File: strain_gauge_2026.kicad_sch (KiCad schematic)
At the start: 34 parts, among them J2 Conn_01x04_Socket, J3 Conn_01x04_Socket, J4 Conn_01x04_Socket, SW1 SW_DIP_x04, U1 NAU7802SGI, U2 LTC4316xDD

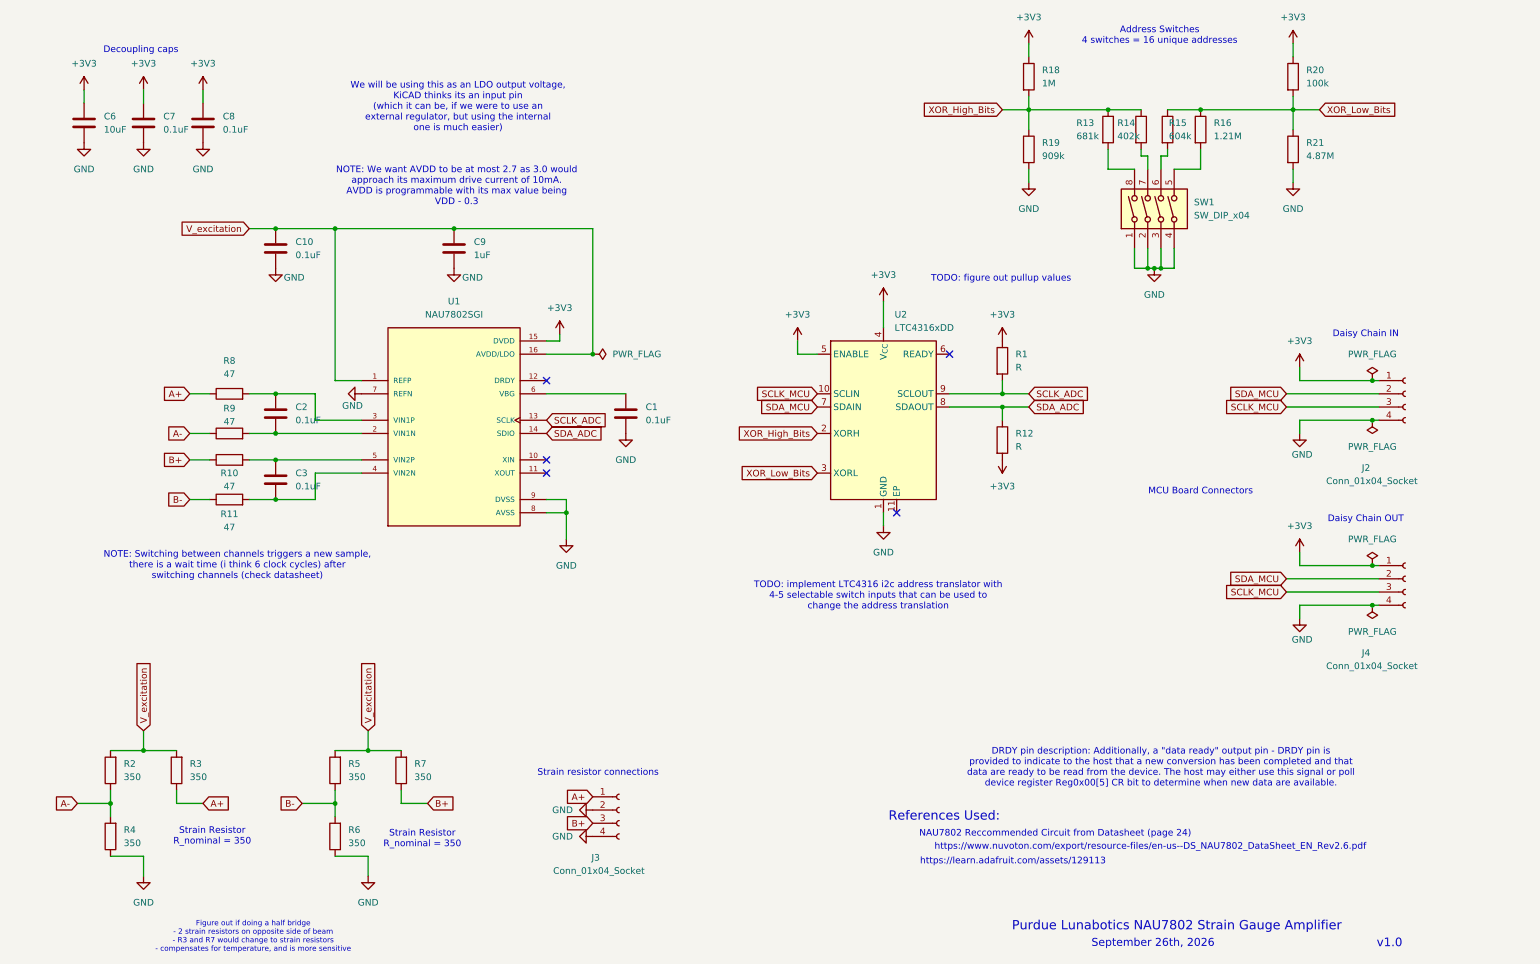
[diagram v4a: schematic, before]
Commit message: Removed LTC4316 from schematic
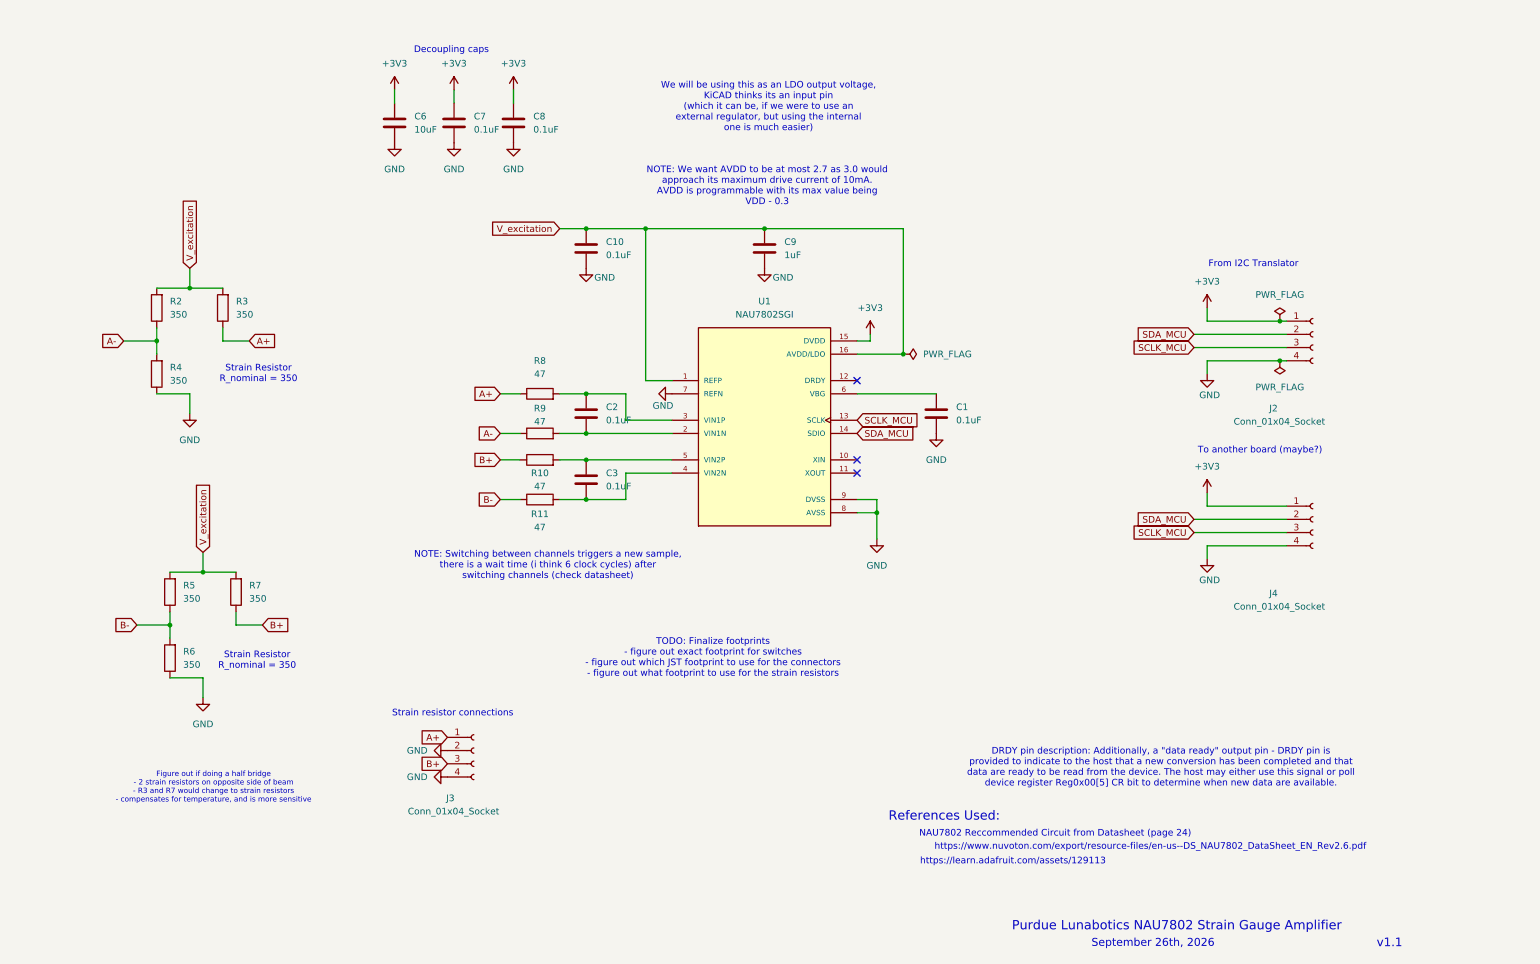
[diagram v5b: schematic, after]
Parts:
- removed R1, R12: R, symbol Device:R
- removed R13: 681k, symbol Device:R
- removed R14: 402k, symbol Device:R
- removed R15: 604k, symbol Device:R
- removed R16: 1.21M, symbol Device:R
- removed R18: 1M, symbol Device:R
- removed R19: 909k, symbol Device:R
- removed R20: 100k, symbol Device:R
- removed R21: 4.87M, symbol Device:R
- removed SW1: SW_DIP_x04, Button_Switch_THT:SW_NKK_GW12LJP, symbol Switch:SW_DIP_x04
- removed U2: LTC4316xDD, Package_DFN_QFN:DFN-10-1EP_3x3mm_P0.5mm_EP1.65x2.38mm, symbol Interface_Expansion:LTC4316xDD
- C1, C10, C2, C3, C7, C8, C9: footprint (none) -> Capacitor_SMD:C_0805_2012Metric_Pad1.18x1.45mm_HandSolder
- C6: footprint (none) -> Capacitor_THT:CP_Radial_D5.0mm_P2.50mm
- J2, J3, J4: footprint Package_DFN_QFN:QFN-20-1EP_5x5mm_P0.65mm_EP3.35x3.35mm -> Connector_PinHeader_2.54mm:PinHeader_1x04_P2.54mm_Vertical
- R10, R11, R2, R3, R4, R5, R6, R7, R8, R9: footprint (none) -> Resistor_SMD:R_0805_2012Metric_Pad1.20x1.40mm_HandSolder
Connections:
- net SCLK_ADC is gone; now on net SCLK_MCU: U1.13 (SCLK)
- net SDA_ADC is gone; now on net SDA_MCU: U1.14 (SDIO)
- no-connect marks 5 -> 3
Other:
- note added: "From I2C Translator"
- note added: "TODO: Finalize footprints - figure out exact footprint for switches - figure out which JST footprint to use for the connectors - figure out what footprint to use for the strain resistors"
- note added: "To another board (maybe?)"
- note added: "v1.1"
- note removed: "Address Switches 4 switches = 16 unique addresses"
- note removed: "Daisy Chain IN"
- note removed: "Daisy Chain OUT"
- note removed: "MCU Board Connectors"
- note removed: "TODO: figure out pullup values"
- note removed: "TODO: implement LTC4316 i2c address translator with 4-5 selectable switch inputs that can be used to change the address translation"
- note removed: "v1.0"
- moved on the sheet: C1, C10, C2, C3, C6, C7, C8, C9, J2, J3, J4, R10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

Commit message: Added optional Half/Quarter bridge connections
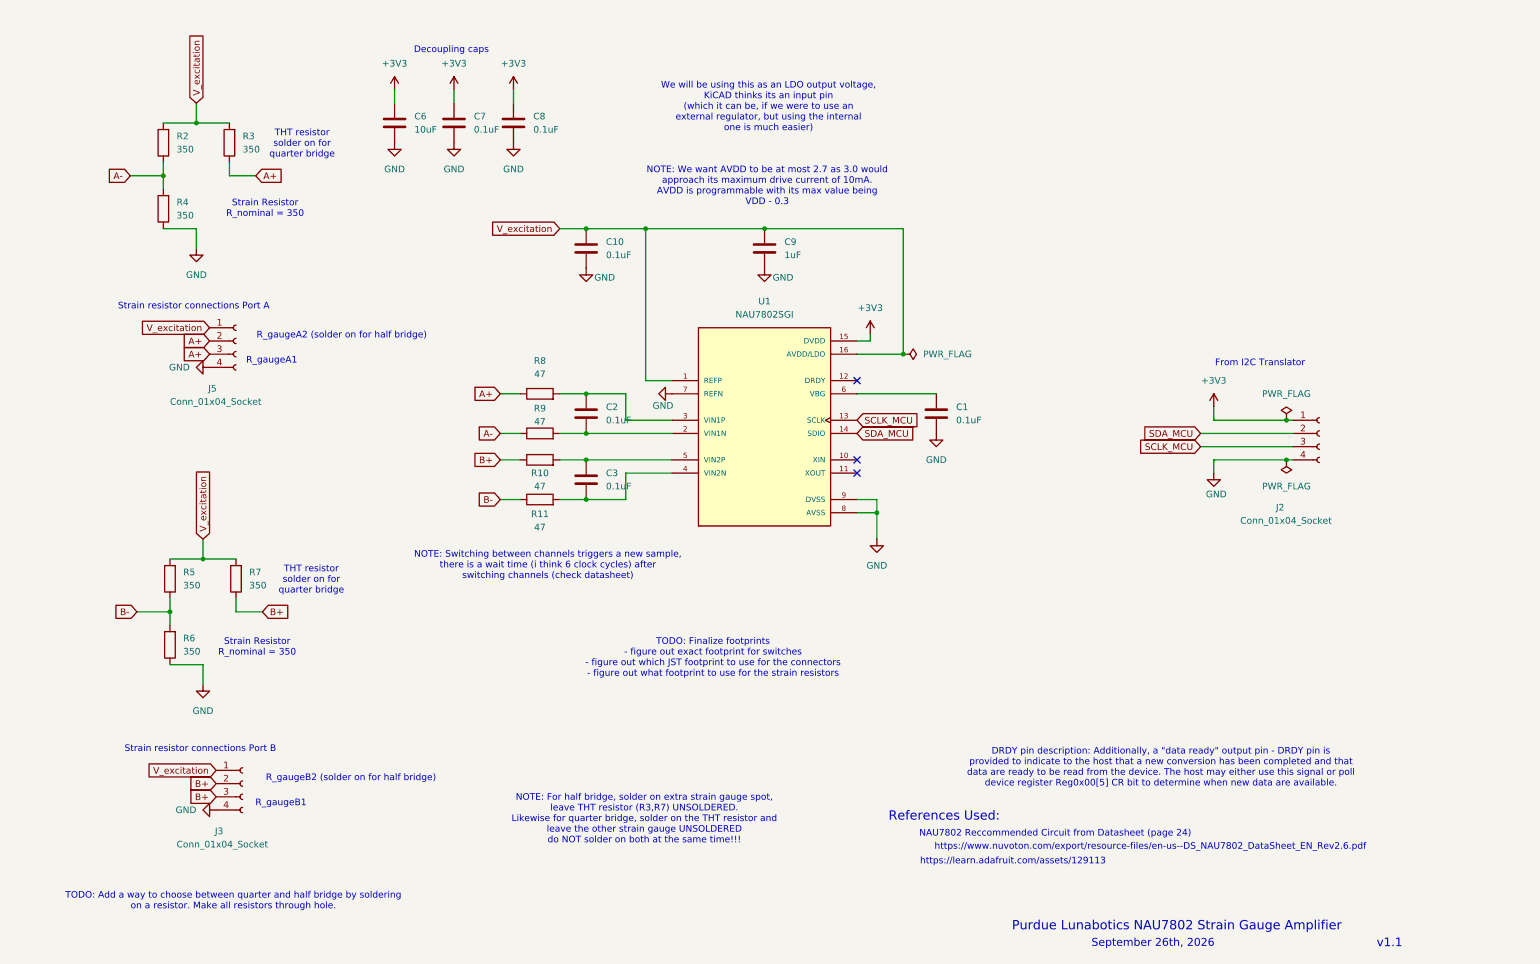
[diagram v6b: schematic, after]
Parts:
- removed J4: Conn_01x04_Socket, Connector_PinHeader_2.54mm:PinHeader_1x04_P2.54mm_Vertical, symbol Connector:Conn_01x04_Socket
- added J5: Conn_01x04_Socket, Connector_PinHeader_2.54mm:PinHeader_1x04_P2.54mm_Vertical, symbol Connector:Conn_01x04_Socket
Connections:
- net A+: now also J5.2 (Pin_2), J5.3 (Pin_3); no longer J3.1 (Pin_1)
- net B+: now also J3.2 (Pin_2)
- net GND: now also J5.4 (Pin_4); no longer J3.2 (Pin_2)
- net V_excitation: now also J3.1 (Pin_1), J5.1 (Pin_1)
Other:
- note added: "NOTE: For half bridge, solder on extra strain gauge spot, leave THT resistor (R3,R7) UNSOLDERED. Likewise for quarter bridge, solder on the THT resistor and leave the other strain gauge UNSOLDERED do NOT solder on both at the same time!!!"
- note added: "R_gaugeA1"
- note added: "R_gaugeA2 (solder on for half bridge)"
- note added: "R_gaugeB1"
- note added: "R_gaugeB2 (solder on for half bridge)"
- note added: "Strain resistor connections Port A"
- note added: "Strain resistor connections Port B"
- note added: "THT resistor solder on for quarter bridge"
- note added: "TODO: Add a way to choose between quarter and half bridge by soldering on a resistor. Make all resistors through hole."
- note removed: "Figure out if doing a half bridge - 2 strain resistors on opposite side of beam - R3 and R7 would change to strain resistors - compensates for temperature, and is more sensitive"
- note removed: "Strain resistor connections"
- note removed: "To another board (maybe?)"
- moved on the sheet: J2, J3, R2, R3, R4, R5, R6, R7

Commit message: Passives selected, footprints assigned accordingly
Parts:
- C6: footprint Capacitor_THT:CP_Radial_D5.0mm_P2.50mm -> Capacitor_THT:CP_Radial_D5.0mm_P2.00mm
- C9: footprint Capacitor_SMD:C_0805_2012Metric_Pad1.18x1.45mm_HandSolder -> Capacitor_THT:C_Rect_L7.0mm_W3.5mm_P5.00mm
- R10, R11, R2, R3, R4, R5, R6, R7, R8, R9: footprint Resistor_SMD:R_0805_2012Metric_Pad1.20x1.40mm_HandSolder -> Resistor_THT:R_Axial_DIN0207_L6.3mm_D2.5mm_P10.16mm_Horizontal
- U1: footprint strain_gauge_footprint_lib:SOIC127P600X175-16N -> Package_DIP:DIP-16_W7.62mm
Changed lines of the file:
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@@
 			)
 		)
-		(property "Footprint" "Resistor_SMD:R_0805_2012Metric_Pad1.20x1.40mm_HandSolder"
+		(property "Footprint" "Resistor_THT:R_Axial_DIN0207_L6.3mm_D2.5mm_P10.16mm_Horizontal"
 			(at 55.118 123.19 90)
 			(hide yes)
@@
 			)
 		)
-		(property "Footprint" "Resistor_SMD:R_0805_2012Metric_Pad1.20x1.40mm_HandSolder"
+		(property "Footprint" "Resistor_THT:R_Axial_DIN0207_L6.3mm_D2.5mm_P10.16mm_Horizontal"
 			(at 53.848 39.37 90)
 			(hide yes)
@@
 			)
 		)
-		(property "Footprint" "Resistor_SMD:R_0805_2012Metric_Pad1.20x1.40mm_HandSolder"
+		(property "Footprint" "Resistor_THT:R_Axial_DIN0207_L6.3mm_D2.5mm_P10.16mm_Horizontal"
 			(at 111.76 109.728 90)
 			(hide yes)
@@
 			)
 		)
-		(property "Footprint" "Capacitor_THT:CP_Radial_D5.0mm_P2.50mm"
+		(property "Footprint" "Capacitor_THT:CP_Radial_D5.0mm_P2.00mm"
 			(at 84.7852 39.37 0)
 			(hide yes)
@@
 			)
 		)
-		(property "Footprint" "Resistor_SMD:R_0805_2012Metric_Pad1.20x1.40mm_HandSolder"
+		(property "Footprint" "Resistor_THT:R_Axial_DIN0207_L6.3mm_D2.5mm_P10.16mm_Horizontal"
 			(at 41.148 39.37 90)
 			(hide yes)
@@
 			)
 		)
-		(property "Footprint" "Resistor_SMD:R_0805_2012Metric_Pad1.20x1.40mm_HandSolder"
+		(property "Footprint" "Resistor_THT:R_Axial_DIN0207_L6.3mm_D2.5mm_P10.16mm_Horizontal"
 			(at 42.418 135.89 90)
 			(hide yes)
@@
 			)
 		)
-		(property "Footprint" "Resistor_SMD:R_0805_2012Metric_Pad1.20x1.40mm_HandSolder"
+		(property "Footprint" "Resistor_THT:R_Axial_DIN0207_L6.3mm_D2.5mm_P10.16mm_Horizontal"
 			(at 111.76 97.028 90)
 			(hide yes)
@@
 			)
 		)
-		(property "Footprint" "Resistor_SMD:R_0805_2012Metric_Pad1.20x1.40mm_HandSolder"
+		(property "Footprint" "Resistor_THT:R_Axial_DIN0207_L6.3mm_D2.5mm_P10.16mm_Horizontal"
 			(at 111.76 102.108 90)
 			(hide yes)
@@
 			)
 		)
-		(property "Footprint" "strain_gauge_footprint_lib:SOIC127P600X175-16N"
+		(property "Footprint" "Package_DIP:DIP-16_W7.62mm"
 			(at 154.94 92.71 0)
 			(hide yes)
@@
 			)
 		)
-		(property "Footprint" "Resistor_SMD:R_0805_2012Metric_Pad1.20x1.40mm_HandSolder"
+		(property "Footprint" "Resistor_THT:R_Axial_DIN0207_L6.3mm_D2.5mm_P10.16mm_Horizontal"
 			(at 42.418 123.19 90)
 			(hide yes)
@@
 			)
 		)
-		(property "Footprint" "Capacitor_SMD:C_0805_2012Metric_Pad1.18x1.45mm_HandSolder"
+		(property "Footprint" "Capacitor_THT:C_Rect_L7.0mm_W3.5mm_P5.00mm"
 			(at 155.9052 63.5 0)
 			(hide yes)
@@
 			)
 		)
-		(property "Footprint" "Resistor_SMD:R_0805_2012Metric_Pad1.20x1.40mm_HandSolder"
+		(property "Footprint" "Resistor_THT:R_Axial_DIN0207_L6.3mm_D2.5mm_P10.16mm_Horizontal"
 			(at 41.148 52.07 90)
 			(hide yes)
@@
 			)
 		)
-		(property "Footprint" "Resistor_SMD:R_0805_2012Metric_Pad1.20x1.40mm_HandSolder"
+		(property "Footprint" "Resistor_THT:R_Axial_DIN0207_L6.3mm_D2.5mm_P10.16mm_Horizontal"
 			(at 111.76 89.408 90)
 			(hide yes)
